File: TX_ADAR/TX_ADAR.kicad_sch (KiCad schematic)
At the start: 8 parts, among them SW2 SW_SPDT, U2 ADAR2001ACCZ

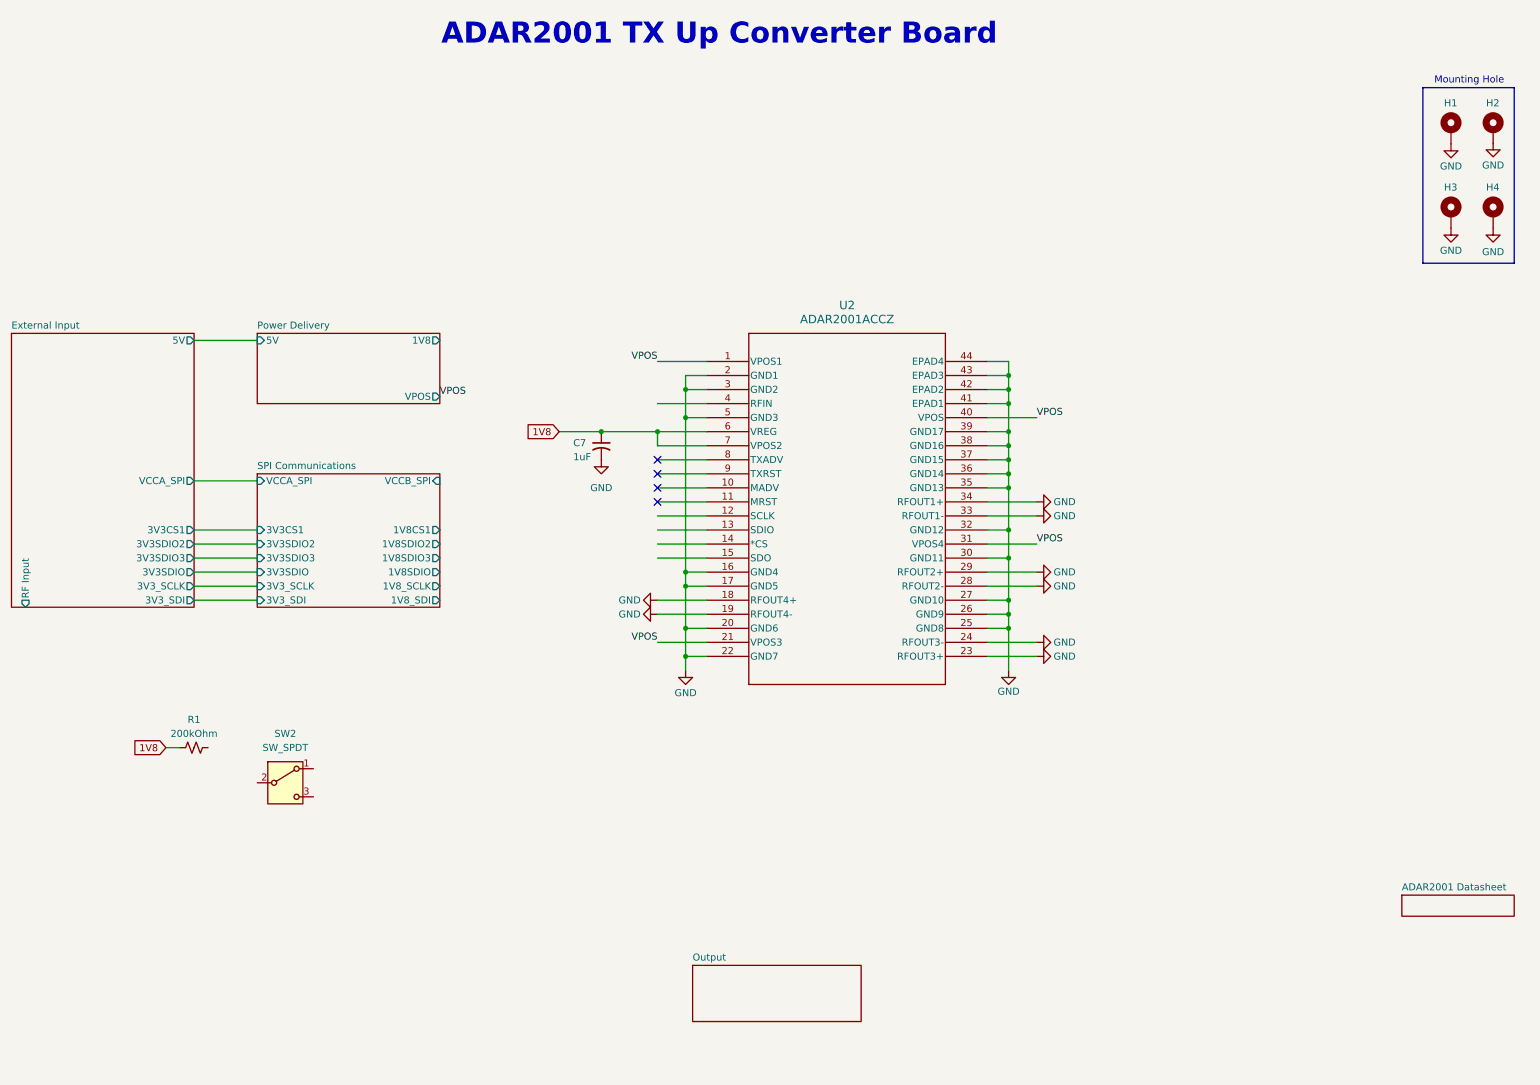
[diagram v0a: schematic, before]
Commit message: After Vccb>Vcca
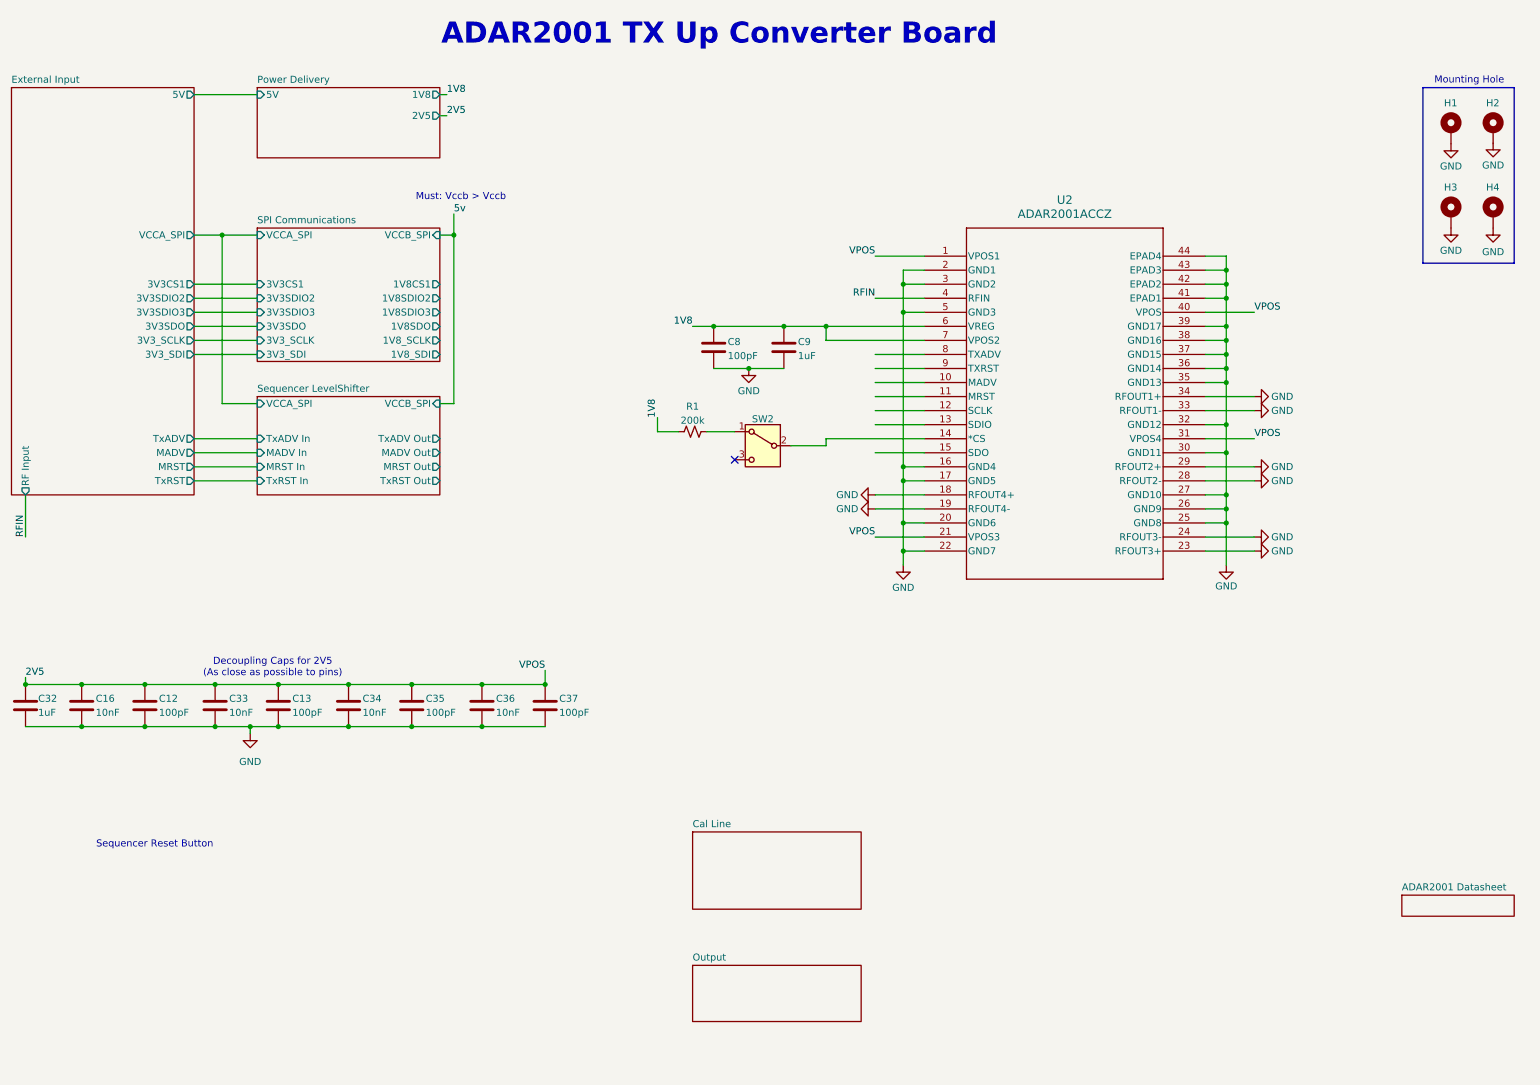
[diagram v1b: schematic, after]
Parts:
- removed C7: 1uF, symbol Device:C_Small_US
- added C12, C13, C35, C37, C8: 100pF, symbol Device:C
- added C16, C33, C34, C36: 10nF, symbol Device:C
- added C32, C9: 1uF, symbol Device:C
- R1: value 200kOhm -> 200k
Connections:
- net 1V8: now also R1.2, C8.1, C9.1; no longer R1.1
- net GND: now also C12.2, C13.2, C16.2, C32.2, C33.2, C34.2, C35.2, C36.2, C37.2, C8.2, C9.2
- net at U2.14 (*CS): now also SW2.2 (B)
- net RFIN: now reaches U2.4 (RFIN)
- net at SW2.1 (A): now also R1.1
- net VPOS renamed 2V5
- net 2V5: now also C12.1, C13.1, C16.1, C32.1, C33.1, C34.1, C35.1, C36.1, C37.1
- no-connect marks 4 -> 1
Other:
- added sheet Cal Line (CalLine.kicad_sch)
- added sheet Sequencer LevelShifter (SequencerLevelShifter.kicad_sch)
- sheet External Input ports: added 3V3SDO, MADV, MRST, TxADV, TxRST; removed 3V3SDIO
- sheet Power Delivery ports: added 2V5; removed VPOS
- sheet SPI Communications ports: added 1V8SDO, 3V3SDO; removed 1V8SDIO, 3V3SDIO
- note added: "Decoupling Caps for 2V5 (As close as possible to pins)"
- note added: "Must: Vccb > Vccb"
- note added: "Sequencer Reset Button"
- moved on the sheet: SW2, U2

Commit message: Moving things around
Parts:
- added J19, J20: Conn_Coaxial, symbol Connector:Conn_Coaxial
- added R5, R6: 50ohm, Resistor_THT:R_Array_SIP4, symbol Device:R_Small_US
- added SW5, SW8: SW_Push, Package_TO_SOT_THT:TO-220-3_Vertical, symbol Switch:SW_Push
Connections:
- net GND: now also R5.2, R6.2; no longer U2.18 (RFOUT4+), U2.19 (RFOUT4-), U2.23 (RFOUT3+), U2.24 (RFOUT3-), U2.28 (RFOUT2-), U2.29 (RFOUT2+), U2.33 (RFOUT1-), U2.34 (RFOUT1+)
- net Sequencer Level Shifter/MRST Out: now also SW8.1
- net Sequencer Level Shifter/TxRST Out: now also SW5.2
- net MADV: now reaches U2.10 (MADV)
- net MADV: now also R6.1
- net MRST: now reaches U2.11 (MRST)
- net MRST: now also SW8.2
- net SCLK: now reaches U2.12 (SCLK)
- net SDIO: now reaches U2.13 (SDIO)
- net SDO: now reaches U2.15 (SDO)
- net TxADV: now reaches U2.8 (TXADV)
- net TxADV: now also R5.1
- net TxRST: now reaches U2.9 (TXRST)
- net TxRST: now also SW5.1
- new net: J19.2 (Ext), J20.2 (Ext)
- new net RFOut1+: U2.34 (RFOUT1+)
- new net RFOut1-: U2.33 (RFOUT1-)
- new net RFOut2+: U2.29 (RFOUT2+)
- new net RFOut2-: U2.28 (RFOUT2-)
- new net RFOut3+: U2.23 (RFOUT3+)
- new net RFOut3-: U2.24 (RFOUT3-)
- new net RFOut4+: U2.18 (RFOUT4+)
- new net RFOut4-: U2.19 (RFOUT4-)
- no-connect marks 1 -> 3
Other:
- sheet Sequencer LevelShifter renamed Sequencer Level Shifter
- removed sheet Cal Line
- sheet External Input ports: added 3V3CSB, 3V3_SDIO; removed 3V3CS1, 3V3_SDI
- sheet Output ports: added Out1+, Out1-, Out2+, Out2-, Out3+, Out3-, Out4+, Out4-; removed none
- sheet SPI Communications ports: added 1V8CSB, 1V8_SDIO, 3V3CSB, 3V3_SDIO; removed 1V8CS1, 1V8_SDI, 3V3CS1, 3V3_SDI
- note added: "Decoupling Caps for 2V5 (1uF for rail) (10nF & 100pF as close as possible to each pin)"
- note added: "Mounting Holes"
- note added: "Terminate Near DUT"
- note added: "Thru Cal Line Length = 2 x RF Output"
- note removed: "Decoupling Caps for 2V5 (As close as possible to pins)"
- note removed: "Mounting Hole"
- note removed: "Must: Vccb > Vccb"
- moved on the sheet: C12, C13, C16, C32, C33, C34, C35, C36, C37, C8, C9, H1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
